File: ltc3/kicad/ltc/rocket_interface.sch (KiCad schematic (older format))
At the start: 68 parts, among them J401 RJ45, K401 RELAY_1C, K402 RELAY_1C, M401 10A, P401 MicroFit header, P402 MicroFit connector, P403 MicroFit header, P404 MicroFit header, P405 XH header, P406 MicroFit header, P407 MicroFit connector, P408 CONN_01x02, P409 XH connector, Q401 PMV45EN, Q402 ZVN4525E6, Q403 ZVN4525E6, Q404 ZVN4525E6, Q405 PMV45EN, SW401 SPST, U401 CD74HC14, U402 SN65220DBV, U403 SN74AHC1G08, U404 TLP3542

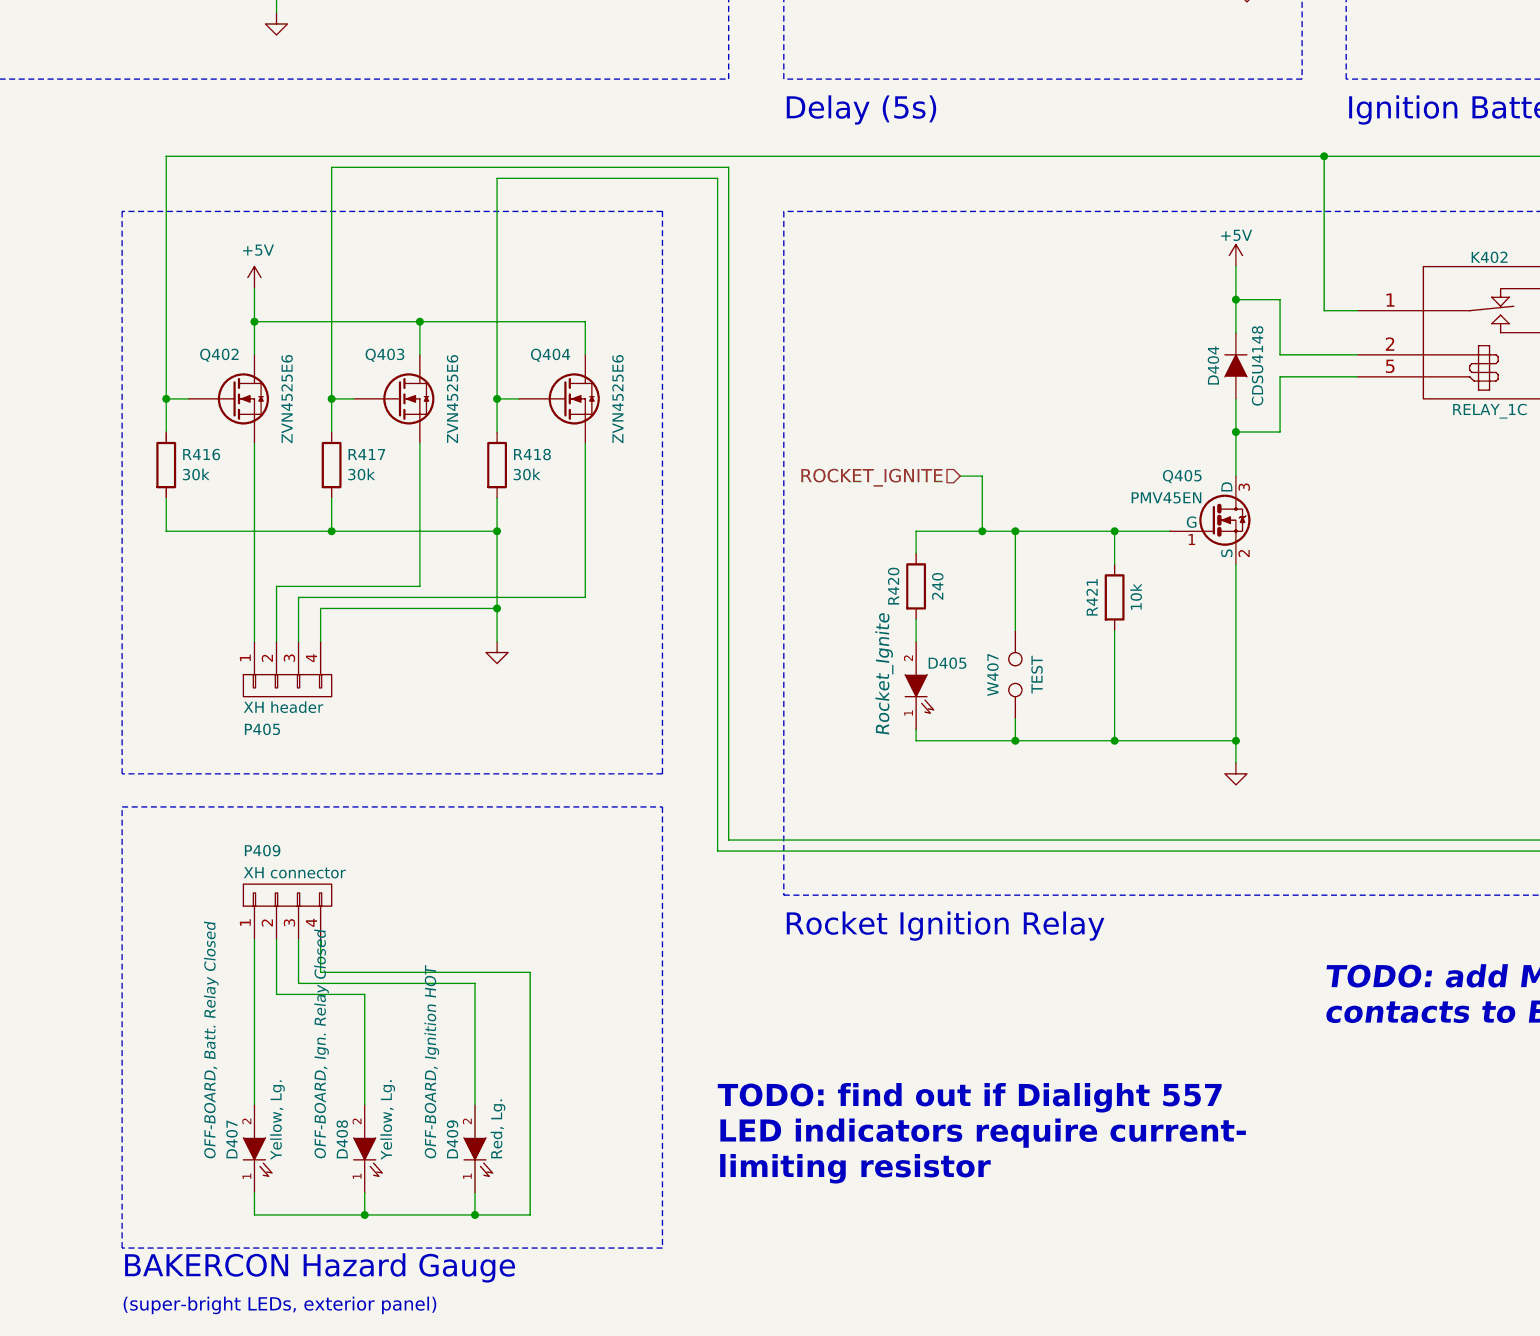
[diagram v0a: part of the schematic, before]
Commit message: LTC3: Added zero-ohm current-limiting resistors to LTC's BAKERCON.
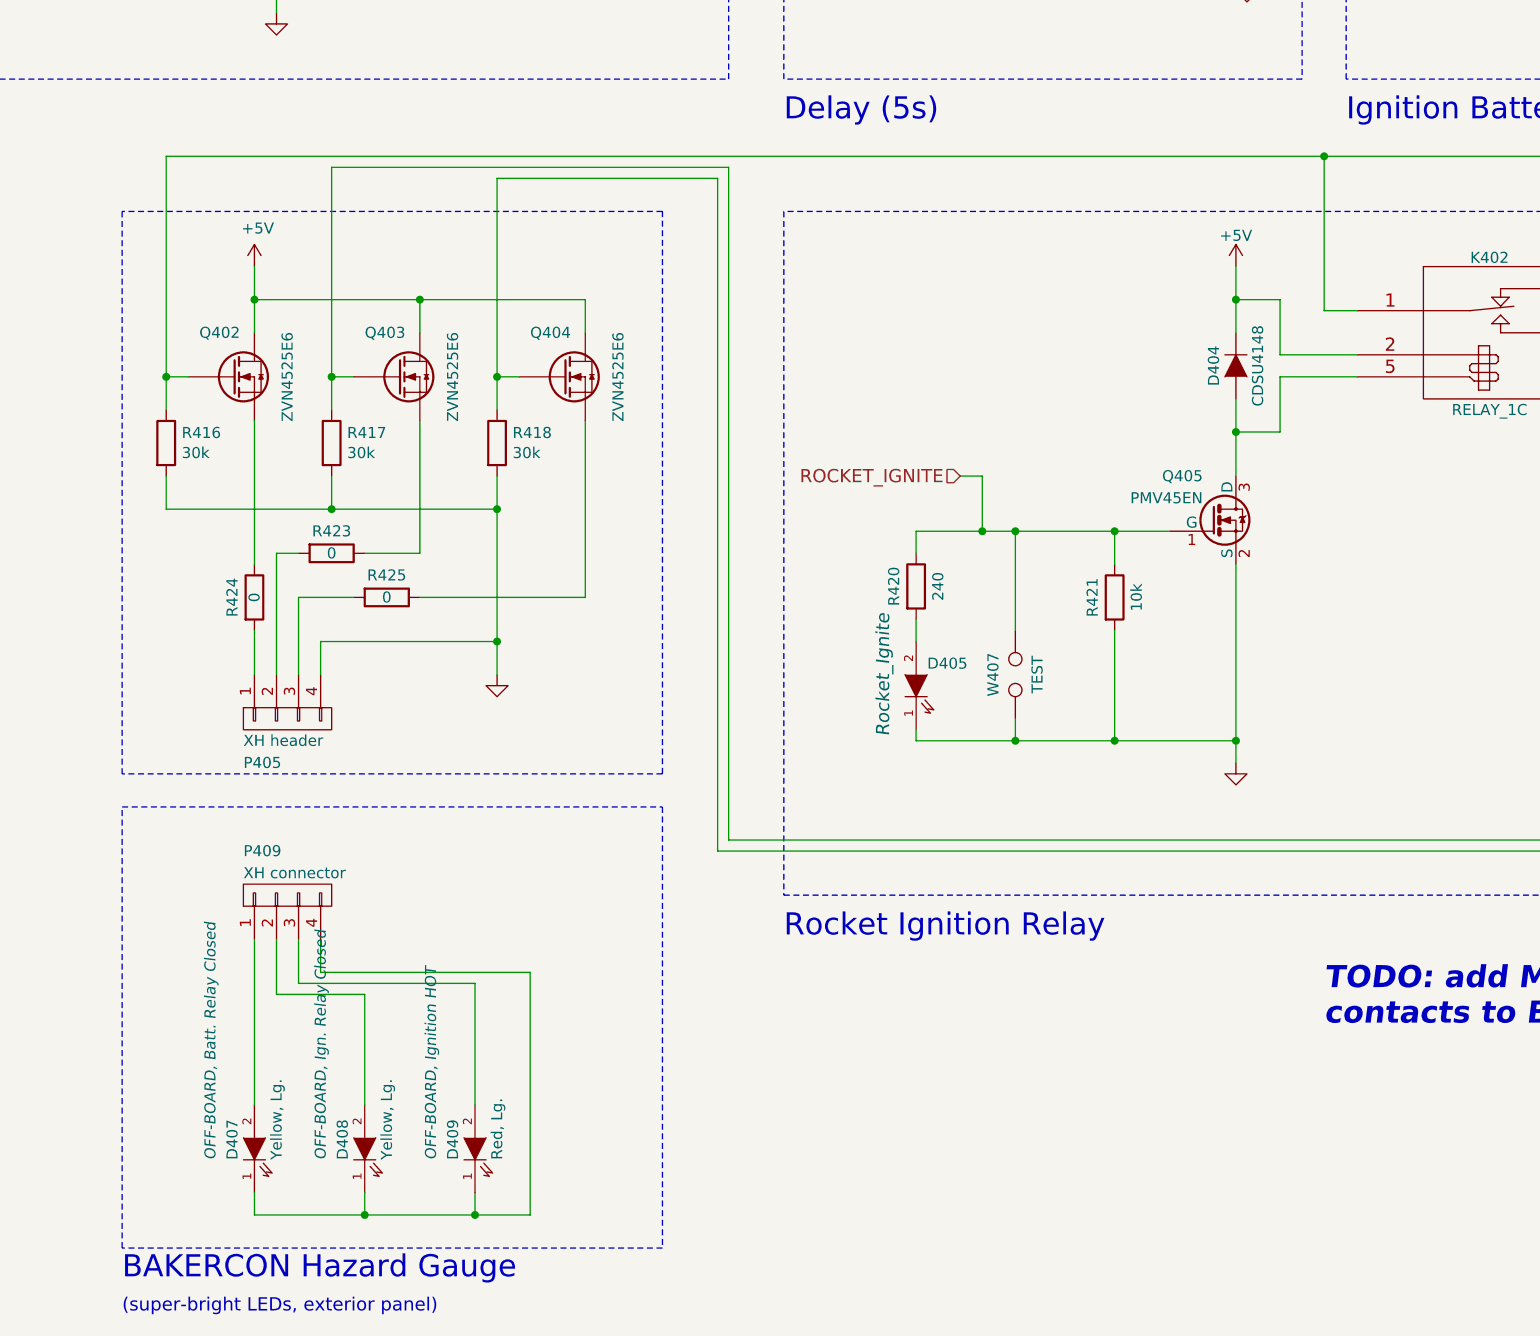
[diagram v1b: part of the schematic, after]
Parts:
- added R423, R424, R425: 0, symbol R
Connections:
- net at P405.1 (P1): now also R424.2; no longer Q402.4 (S)
- net at P405.2 (P2): now also R423.2; no longer Q403.4 (S)
- net at P405.3 (P3): now also R425.2; no longer Q404.4 (S)
- new net: Q402.4 (S), R424.1
- new net: Q403.4 (S), R423.1
- new net: Q404.4 (S), R425.1
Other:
- note removed: "TODO: find out if Dialight 557\nLED indicators require current-\nlimiting resistor"
- moved on the sheet: P405, Q402, Q403, Q404, R416, R417, R418

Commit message: LTC3: Doubled pin count of LTC's DC in and ignition battery connectors.
Using the same 4-pin Molex MicroFit as used for battery connection on
Charge Controller and Cell Protection boards.
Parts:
- P401: footprint Connectors_Molex:Molex_Microfit3_Header_02x01_Straight_43045-0228 -> Connectors_Molex:Molex_Microfit3_Header_02x02_Straight_43045-0428; symbol CONN_01X02 -> CONN_01X04; Mfg_Description 2 pos vertical header -> 4 pos vertical header; Mfg_PN 43045-0228 -> 43045-0428
- R423, R424, R425: footprint (none) -> Resistors_SMD:R_0805; Mfg_Description (none) -> 1/8W; Mfg_Name (none) -> Yageo; Mfg_PN (none) -> RC0805JR-070RL; Note (none) -> Dialight LED may not require ext. R; Spec (none) -> -
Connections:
- net GND_IGN: now also P401.3 (P3), P401.4 (P4); no longer P401.2 (P2)
- net IGN_BATT_P: now also P401.2 (P2)

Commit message: LTC3: LTC BOM and PCB changes.
1. Added RJ45 connector outline to BeagleBone footprint.

2. Rotated BeagleBone footprint on PCB, so that the RJ45 connector
   is on a board edge.

3. Added a notch to the board for BeagleBone RJ45 jack clearance.

4. Updated PCB footprint annotations to align with changes made to the
   LTC schematic in the past few months.

5. Changed BAKERCON MOSFETs to be same part used to activate ignition
   relays.  (Fewer distinct components on the board.)
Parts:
- P402: renamed from P403; Note to front panel -> to front panel; mates to P403
- P403: renamed from P402; Note OFF-BOARD; mates to P403 -> OFF-BOARD; mates to P402
- P404: renamed from P406; Note to front panel -> to front panel; mates to P405
- P405: renamed from P407; Note OFF-BOARD; mates to P406 -> OFF-BOARD; mates to P404
- P406: renamed from P405; footprint Connectors_JST:JST_XH_B04B-XH-A_02x2.50mm_Straight -> Connectors_JST:JST_XH_B04B-XH-A_04x2.50mm_Straight; Note to front panel -> to front panel; mates to P407
- P407: renamed from P409; Note OFF-BOARD; mates to P405 -> OFF-BOARD; mates to P406
- Q401: Mfg_PN PMV45EN -> PMV45EN2R
- Q402, Q403, Q404: value ZVN4525E6 -> PMV45EN; footprint TO_SOT_Packages_SMD:SOT-23-6 -> TO_SOT_Packages_SMD:SOT-23; symbol Q_NMOS_SOT26 -> PMV45EN; Mfg_Description MOSFET N-CH 250V 230MA -> MOSFET N-CH 30V; Mfg_Name Diodes, Inc. -> NXP; Mfg_PN ZVN4525E6TA -> PMV45EN2R
- R416, R417, R418: value 30k -> 10k; Mfg_PN RC0805FR-0730KL -> RC0805FR-0710KL
- renumbered P404 to P408, P408 to P409
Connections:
- net +5V: now also Q402.3 (D), Q403.3 (D), Q404.3 (D); no longer Q402.1 (D), Q403.1 (D), Q404.1 (D)
- net at K401.3 (NO), K402.1 (COM), R416.1: now also Q402.1 (G); no longer Q402.3 (G)
- net at K402.3 (NO), P402.1 (P1), R417.1: now also Q403.1 (G); no longer Q403.3 (G)
- net at P402.2 (P2), P404.1 (P1), R418.1: now also Q404.1 (G); no longer Q404.3 (G)
- net at Q402.2 (S): now also R424.1
- net at Q403.2 (S): now also R423.1
- net at Q404.2 (S): now also R425.1
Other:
- moved on the sheet: JP401, M401, P403, SW401

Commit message: Converted LTC schematic from KiCad v4 to v5.
v5 schematic exported as PDF to
build/schematics/3-Launch_Tower_Computer-KiCad_v5.pdf to simplify
comparison and sanity-checking versus the v4 version at
build/schematics/3-Launch_Tower_Computer.pdf.  New version should be
mv'd overtop of old version before merging this branch to *master*.
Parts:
- C401, C402, C403, C404, C405, C406: symbol C -> Device:C
- D401, D402, D404: symbol D -> Device:D
- D403, D405, D407, D408, D409: symbol LED -> Device:LED
- D406: symbol ZENER -> Device:D_Zener
- J401: symbol RJ45 -> Connector:RJ45_Shielded
- JP401: symbol Jumper_NC_Small -> Device:Jumper_NC_Small
- K401, K402: symbol RELAY_1C -> relay_1c:RELAY_1C
- M401: symbol BREAKER_1P -> breakers:BREAKER_1P
- P401, P406, P407: symbol CONN_01X04 -> Connector:Conn_01x04_Male
- P402, P403, P404, P405, P409: symbol CONN_01X02 -> Connector:Conn_01x02_Male
- P408: symbol CONN_01X10 -> Connector:Conn_01x10_Male
- Q401, Q402, Q403, Q404, Q405: symbol PMV45EN -> PMV45EN:PMV45EN
- R401, R402, R403, R404, R405, R406, R407, R408, R409, R410, R411, R412, R413, R414, R415, R416, R417, R418, R419, R420, R421, R422, R423, R424, R425: symbol R -> Device:R
- SW401: symbol SPST -> switches2:SPST
- U401: symbol CD74HC14 -> CD74HC14:CD74HC14
- U402: symbol SN65220DBV -> SNx52x0:SN65220DBV
- U403: symbol 741G08 -> 741g08:741G08
- U404: symbol TLP3542 -> TLP:TLP3542
- W401, W402, W403, W404, W405, W406, W407: symbol TEST -> Connector:TestPoint_2Pole
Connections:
- net GND: now also J401.SH; no longer J401.9 (SHIELD)
- net GND_IGN: now also W401.2; no longer W401.1
- net IGN_BATT_P: now also W401.1; no longer W401.2
- net at SW401.1: now also M401.1; no longer JP401.1
- net at SW401.2: now also JP401.1; no longer M401.1
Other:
- moved on the sheet: J401
